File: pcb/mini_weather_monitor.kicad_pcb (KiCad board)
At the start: 2 copper layers, 135 x 72 mm, 12 parts, among them J1 SW-520D, U2 4.0inch_SPI_MSP4021, U2_BME280 module_bme280, U3_BH1750 module_bh1750

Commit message: revamping a bit
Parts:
- removed J1: SW-520D, tilt:KY020 Tilt
- removed Ue: PowerSupplyMB102_v13, power_supplies:POWERSUPPLYMB102
- added 5V_buck_boost1: ~, regulator_voltage:S09_HVN, B.Cu at (147.8, 100.5)
- added USB_C_Input1: ~, custom_usbc:USB_C_breakout_power_only, B.Cu at (160.2, 100.0)
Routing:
- net +3V3: track 169.0 -> 77.9 mm, vias 5 -> 2
- net GND: track 316.4 -> 265.4 mm
- net Net-(J1-Pin_1): track 37.7 -> 0.00 mm, vias 1 -> 0
- net VCC_PRE: track 0.00 -> 31.3 mm, vias 0 -> 1
- net VCC: track 178.4 -> 180.8 mm, vias 2 -> 3
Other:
- board text added: "amefuri kozo v0.8 indoor weather monitor onigaku.key.labo @ 10/2024"
- board text removed: "amefuri kozo v0.6 indoor weather monitor onigaku.key.labo @ 6/2022"

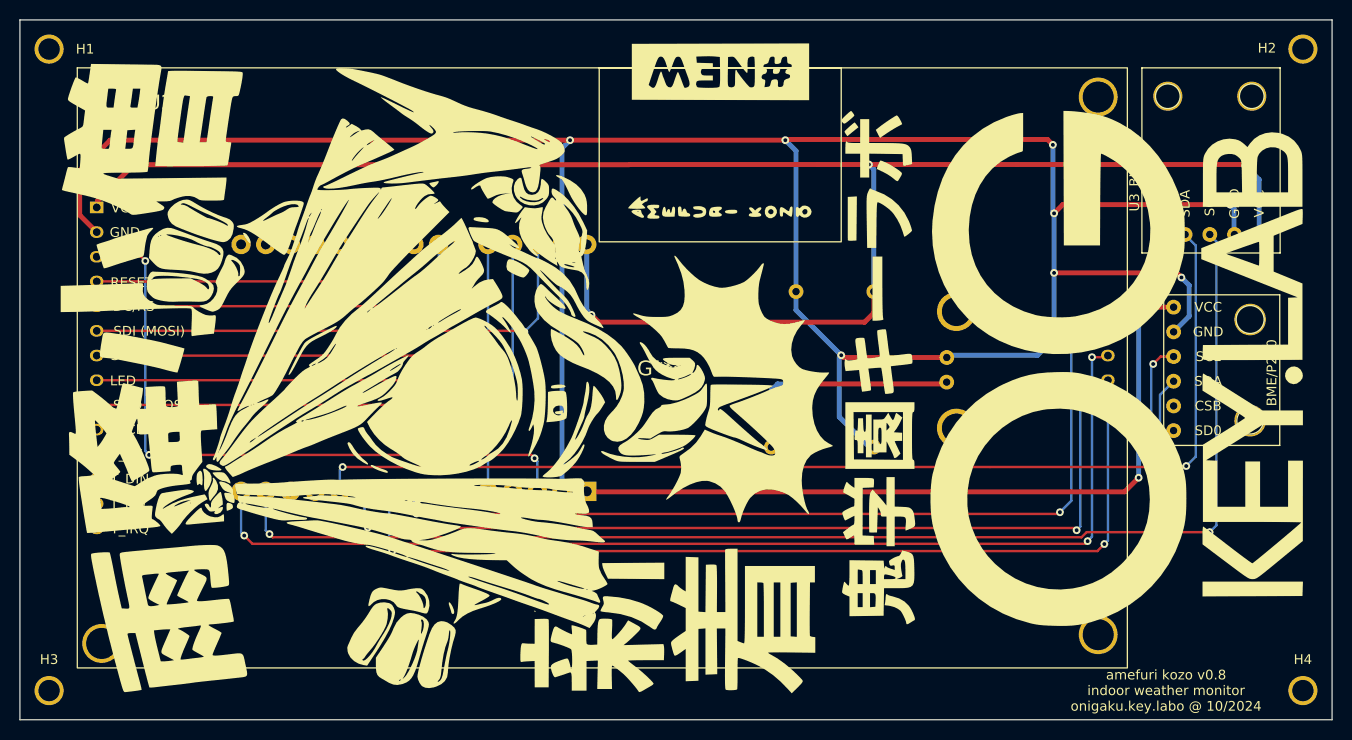
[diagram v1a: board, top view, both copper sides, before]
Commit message: adding extra usb input
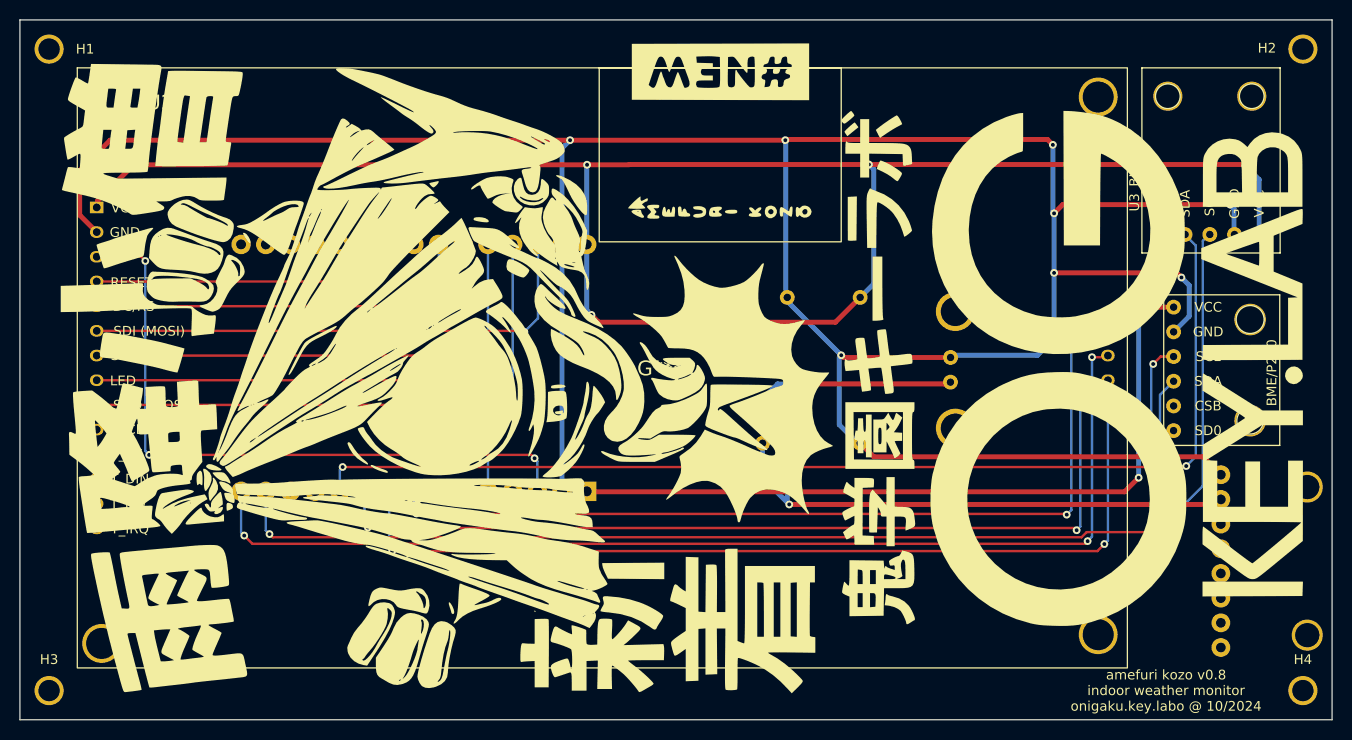
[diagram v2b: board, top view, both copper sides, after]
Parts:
- added adafruit_type_c_downstream1: ~, custom_usbc:Adafruit USB Type C Breakout rev B, B.Cu at (194.0, 119.8)
- moved USB_C_Input1 0.11 mm to (160.1, 100.0)
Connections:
- net VCC_PRE renamed Net-(5V_buck_boost1-EN)
- U_ESP32_DEVKIT_V1 pad 4: Net-(J1-Pin_1) -> unconnected-(U_ESP32_DEVKIT_V1-D2-Pad4)
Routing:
- net Net-(5V_buck_boost1-EN): track 31.3 -> 89.1 mm, vias 1 -> 2
- net GND: track 265.4 -> 303.0 mm
- net VCC: track 180.8 -> 187.3 mm, vias 3 -> 4
- net Net-(U2_BME280-SCL): track 152.7 -> 148.9 mm, vias 4 -> 3
- net Net-(U2-SD_CS): track 90.6 -> 91.2 mm

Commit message: using adafruit stuff
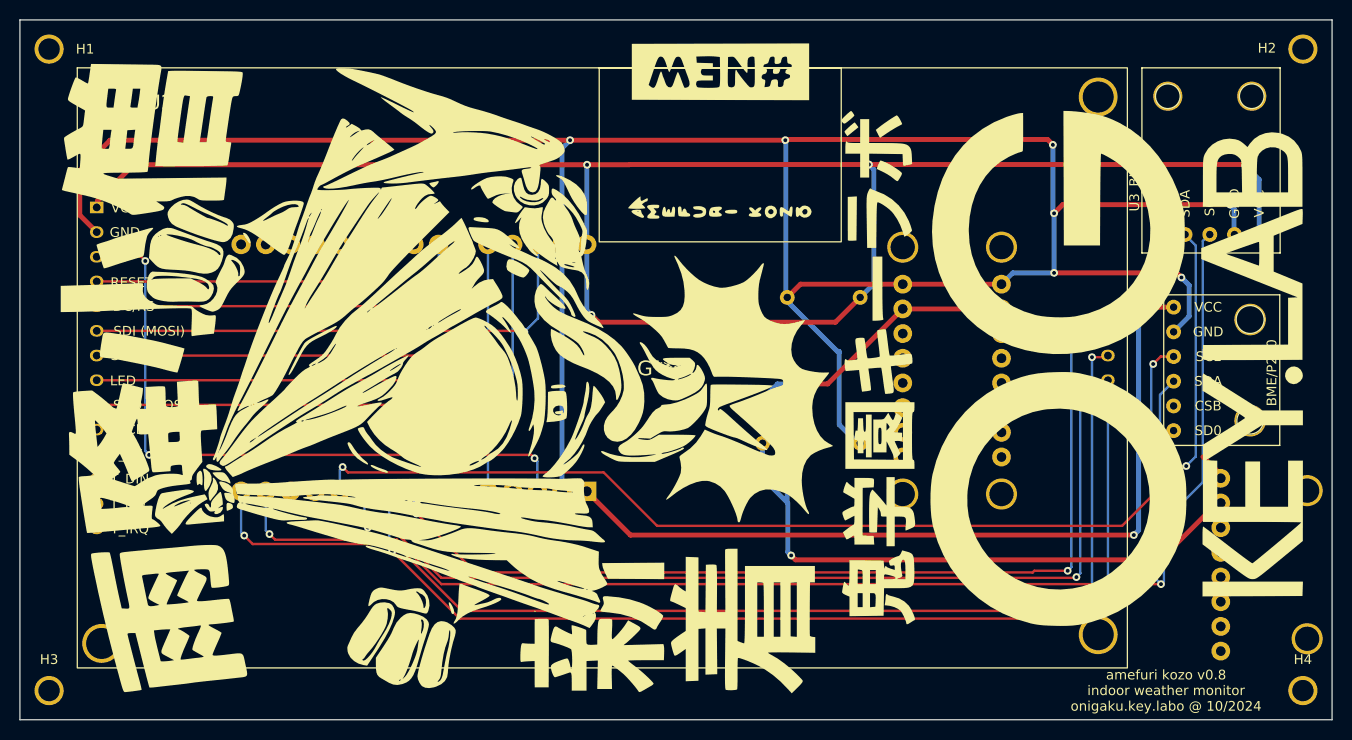
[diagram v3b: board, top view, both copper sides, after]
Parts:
- removed USB_C_Input1: ~, custom_usbc:USB_C_breakout_power_only
- removed adafruit_type_c_downstream1: ~, custom_usbc:Adafruit USB Type C Breakout rev B
- added adafruit_type_c_breakout_rev_b1: ~, custom_usbc:Adafruit_USB_Type_C_Breakout_rev_B, B.Cu at (194.0, 120.2)
- added adafruit_type_c_vertical_breakout1: ~, custom_usbc:Adafruit_USB_Type_C_Vertical_Breakout, B.Cu at (162.0, 100.1)
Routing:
- net GND: track 303.0 -> 266.3 mm, vias 8 -> 7
- net Net-(5V_buck_boost1-EN): track 89.1 -> 105.2 mm
- net Net-(U2_BME280-SCL): track 148.9 -> 162.0 mm
- net Net-(U2-SD_SCK): track 94.3 -> 103.6 mm
- net Net-(U2-SD_MOSI): track 113.0 -> 121.8 mm
- net Net-(U2-SD_CS): track 91.2 -> 99.6 mm
- net Net-(U2-SD_MISO): track 95.1 -> 101.9 mm
- net +3V3: track 77.9 -> 84.8 mm
- net Net-(U2_BME280-SDA): track 123.5 -> 129.8 mm

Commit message: adding caps and diodes
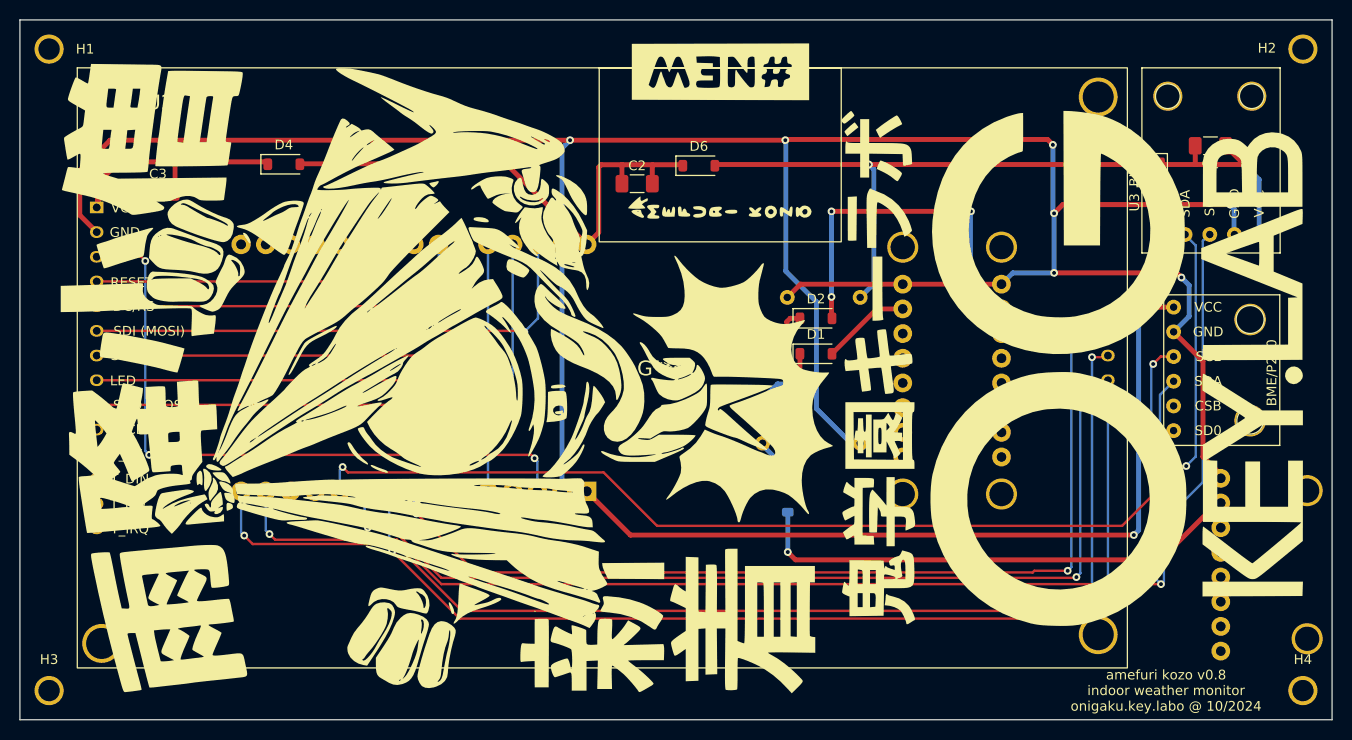
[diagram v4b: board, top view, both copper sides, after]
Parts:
- added C1: C_Small, Capacitor_SMD:C_1206_3216Metric_Pad1.33x1.80mm_HandSolder, F.Cu at (188.5, 77.0)
- added C2: C_Small, Capacitor_SMD:C_1206_3216Metric_Pad1.33x1.80mm_HandSolder, F.Cu at (129.5, 80.8)
- added C3: C_Small, Capacitor_SMD:C_1206_3216Metric_Pad1.33x1.80mm_HandSolder, F.Cu at (80.2, 81.7)
- added D1: 1N5819, Diode_SMD:D_SOD-123, F.Cu at (147.9, 98.3)
- added D2: 1N5819, Diode_SMD:D_SOD-123, F.Cu at (147.9, 94.7)
- added D3: 1N5819, Diode_SMD:D_SOD-123, B.Cu at (145.0, 113.0)
- added D4: 1N5819, Diode_SMD:D_SOD-123, F.Cu at (93.2, 78.8)
- added D5: 1N5819, Diode_SMD:D_SOD-123, F.Cu at (181.7, 78.8)
- added D6: 1N5819, Diode_SMD:D_SOD-123, F.Cu at (135.8, 79.0)
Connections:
- U2 pad 1: VCC -> Net-(D4-K)
- U3_BH1750 pad 5: VCC -> Net-(D5-K)
- adafruit_type_c_breakout_rev_b1 pad 2: Net-(5V_buck_boost1-EN) -> Net-(D3-A)
- adafruit_type_c_vertical_breakout1 pad 10: Net-(5V_buck_boost1-EN) -> Net-(D2-A)
- adafruit_type_c_vertical_breakout1 pad 2: Net-(5V_buck_boost1-EN) -> Net-(D1-A)
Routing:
- net VCC: track 187.3 -> 111.9 mm, vias 4 -> 1
- net Net-(5V_buck_boost1-EN): track 105.2 -> 32.4 mm, vias 2 -> 1
- net Net-(D3-A): track 0.00 -> 52.2 mm, vias 0 -> 1
- net Net-(D2-A): track 0.00 -> 38.6 mm, vias 0 -> 4
- net Net-(D4-K): track 0.00 -> 29.3 mm
- net Net-(D5-K): track 0.00 -> 21.6 mm, vias 0 -> 1
- net GND: track 266.3 -> 280.7 mm
- net Net-(D1-A): track 0.00 -> 9.19 mm

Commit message: working code. pcb wip
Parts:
- removed 5V_buck_boost1: ~, regulator_voltage:S09_HVN
- removed D2, D3, D4, D5, D6: 1N5819, Diode_SMD:D_SOD-123
- added C4: 100nF, Capacitor_SMD:C_1206_3216Metric_Pad1.33x1.80mm_HandSolder, B.Cu at (178.3, 91.5)
- added C5: 10uF, Capacitor_SMD:C_1206_3216Metric_Pad1.33x1.80mm_HandSolder, F.Cu at (130.2, 91.6)
- added C6: 10uF, Capacitor_SMD:C_1206_3216Metric_Pad1.33x1.80mm_HandSolder, F.Cu at (83.4, 77.7)
- added C7: 10uF, Capacitor_SMD:C_1206_3216Metric_Pad1.33x1.80mm_HandSolder, B.Cu at (181.7, 91.5)
- added C8: 10uF, Capacitor_SMD:C_1206_3216Metric_Pad1.33x1.80mm_HandSolder, F.Cu at (183.2, 81.2)
- added J1: Conn_01x02, Connector_PinHeader_2.54mm:PinHeader_1x02_P2.54mm_Vertical, B.Cu at (96.4, 124.7)
- added Q1: IRLML6402, Package_TO_SOT_SMD:SOT-23, B.Cu at (161.6, 124.1)
- added R2: 1k, Resistor_SMD:R_1206_3216Metric, F.Cu at (136.2, 99.1)
- added U1: ~, boost_converter:Pololu U3V70F5, B.Cu at (134.9, 120.1)
- C1, C2, C3: value C_Small -> 100nF
- D1: footprint Diode_SMD:D_SOD-123 -> Diode_SMD:D_SMB
- moved D1 20.6 mm to (129.4, 107.6)
- moved C2 11.2 mm to (126.2, 91.5), turned to -90 degrees
- moved C1 4.33 mm to (188.1, 81.3), turned to -90 degrees
- moved C3 4.16 mm to (79.0, 77.7), turned to 90 degrees
- moved U_ESP32_DEVKIT_V1 3.15 mm to (105.7, 99.8)
- moved adafruit_type_c_vertical_breakout1 2.00 mm to (164.0, 100.1)
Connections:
- C1 pad 1: Net-(D5-K) -> VCC
- C1 pad 2: Net-(D5-K) -> GND
- C2 pad 2: VCC -> GND
- C3 pad 1: Net-(D4-K) -> VCC
- C3 pad 2: Net-(D4-K) -> GND
- D1 pad 1: Net-(5V_buck_boost1-EN) -> VBUS
- U2 pad 1: Net-(D4-K) -> VCC
- U3_BH1750 pad 5: Net-(D5-K) -> VCC
- U_ESP32_DEVKIT_V1 pad 12: unconnected-(U_ESP32_DEVKIT_V1-RX0-Pad12) -> Net-(J1-Pin_1)
- U_ESP32_DEVKIT_V1 pad 13: unconnected-(U_ESP32_DEVKIT_V1-TX0-Pad13) -> Net-(J1-Pin_2)
- adafruit_type_c_breakout_rev_b1 pad 2: Net-(D3-A) -> Net-(Q1-D)
- adafruit_type_c_vertical_breakout1 pad 10: Net-(D2-A) -> Net-(Q1-D)
- adafruit_type_c_vertical_breakout1 pad 2: Net-(D1-A) -> Net-(Q1-D)
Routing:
- net GND: track 280.7 -> 0.69 mm, vias 7 -> 0
- net Net-(Q1-D): track 0.00 -> 71.4 mm, vias 0 -> 2
- net Net-(D3-A): track 52.2 -> 0.00 mm, vias 1 -> 0
- net VCC: track 111.9 -> 163.7 mm, vias 1 -> 5
- net VBUS: track 0.00 -> 44.9 mm, vias 0 -> 2
- net Net-(D2-A): track 38.6 -> 0.00 mm, vias 4 -> 0
- net Net-(5V_buck_boost1-EN): track 32.4 -> 0.00 mm, vias 1 -> 0
- net Net-(D4-K): track 29.3 -> 0.00 mm
- net Net-(D5-K): track 21.6 -> 0.00 mm, vias 1 -> 0
- net +3V3: track 84.8 -> 103.3 mm
- net Net-(U2_BME280-SCL): track 162.0 -> 179.9 mm, vias 3 -> 2
- net Net-(J1-Pin_1): track 0.00 -> 13.5 mm
- net Net-(J1-Pin_2): track 0.00 -> 13.5 mm
- net Net-(D1-A): track 9.19 -> 0.00 mm
- net Net-(U2-SD_CS): track 99.6 -> 108.0 mm
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- added copper zone on B.Cu, net GND
- added copper zone on F.Cu, net GND
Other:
- outline, holes or cut-outs redrawn
- board text added: "RX TX"
- board text added: "amefuri kozo v1.0b indoor weather monitor onigaku.key.labo @ 1/2025"
- board text removed: "amefuri kozo v0.8 indoor weather monitor onigaku.key.labo @ 10/2024"

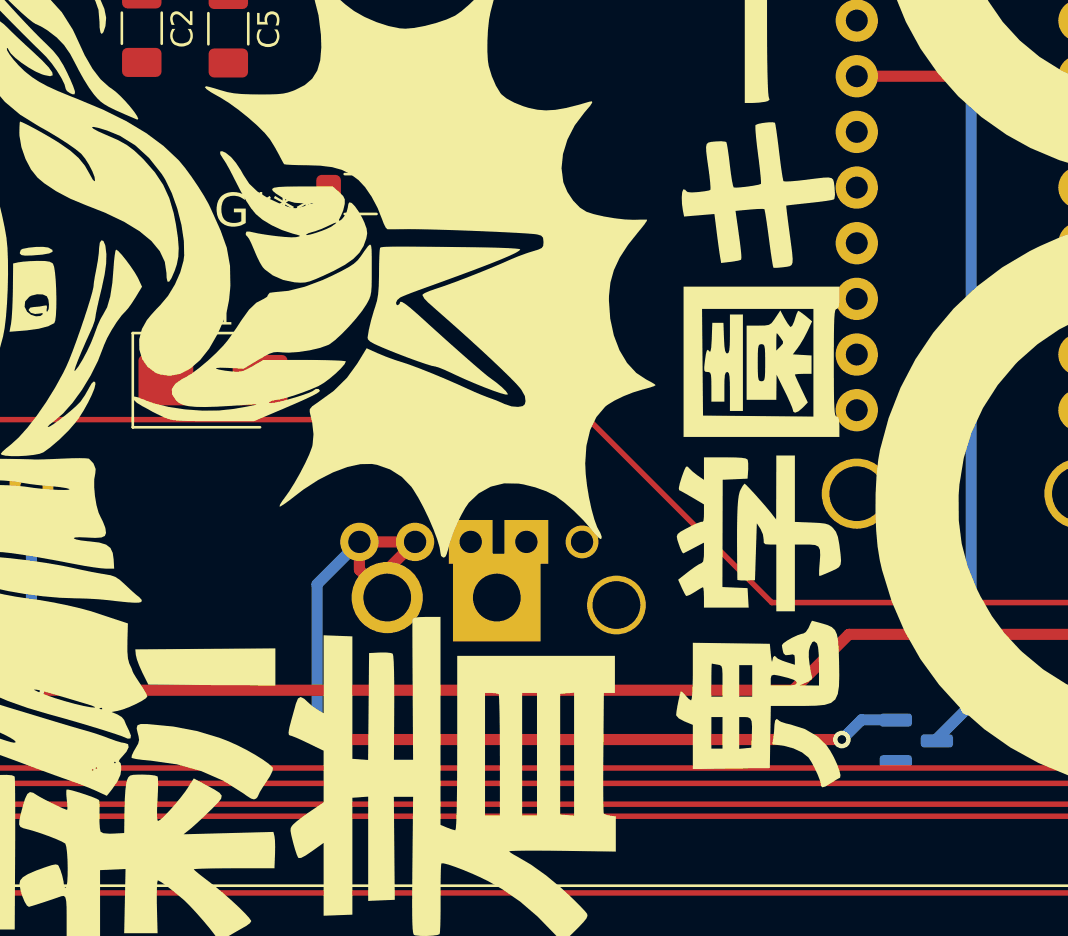
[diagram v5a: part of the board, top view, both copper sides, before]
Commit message: set mosfet, schottkey and resistor
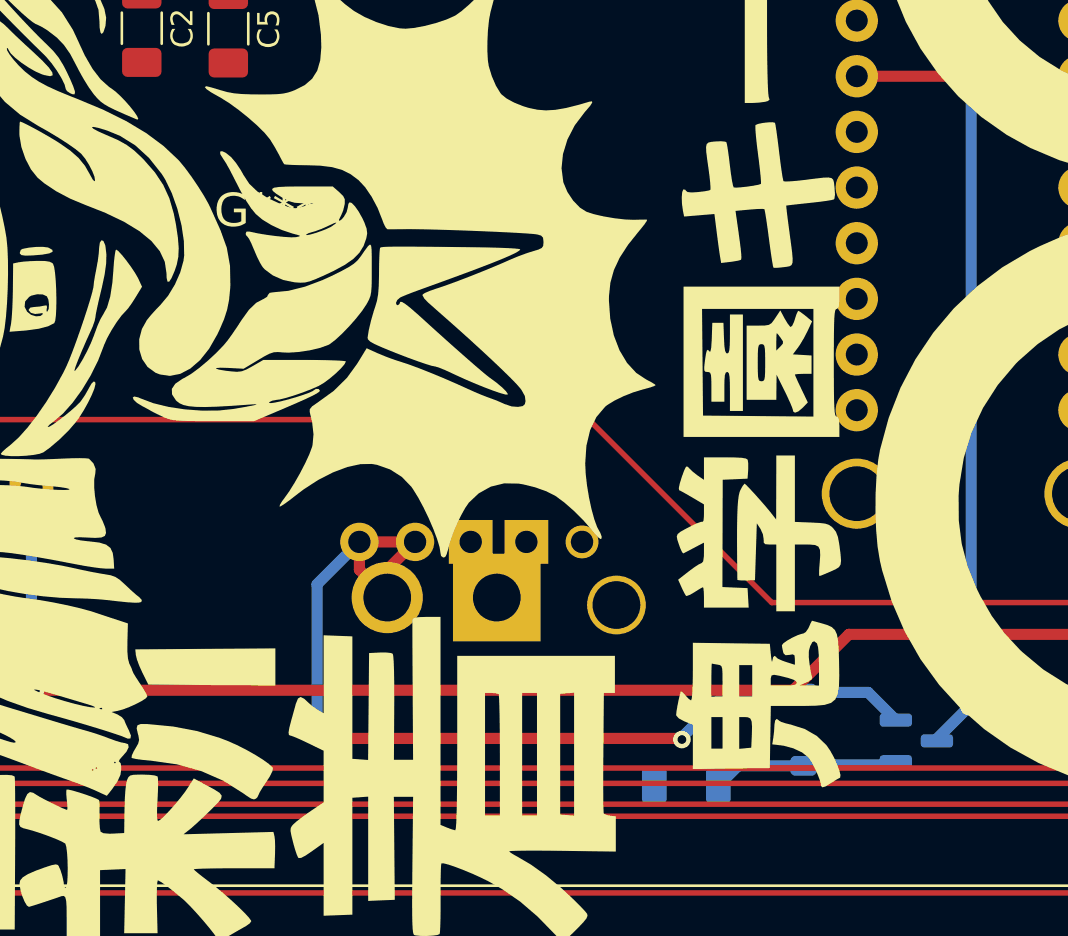
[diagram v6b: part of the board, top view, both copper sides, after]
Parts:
- D1: footprint Diode_SMD:D_SMB -> Diode_SMD:D_SOD-123; moved to B.Cu
- R2: moved to B.Cu
- moved D1 31.3 mm to (156.4, 123.5), turned to -90 degrees
- moved R2 30.8 mm to (151.1, 126.1), turned to 180 degrees
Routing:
- net Net-(D1-A): track 0.00 -> 8.55 mm
- net VBUS: track 44.9 -> 46.3 mm
